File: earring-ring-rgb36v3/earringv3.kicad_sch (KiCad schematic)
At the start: 60 parts, among them J1 Conn_01x05, SW1 SW_Push, SW2 SW_Push, U1 STM32U073KCUx, U2 GMA2718H09-F42-4P

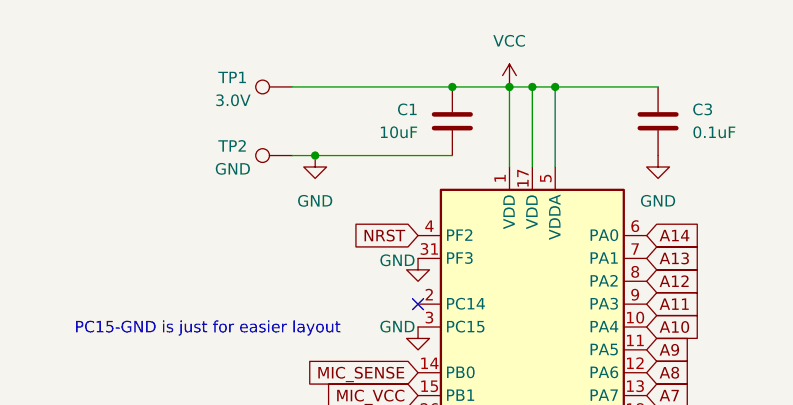
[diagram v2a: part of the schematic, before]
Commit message: earring-ring-rgb36v3: add extra capacitor
The datasheet says this capacitor is needed so :shrug:
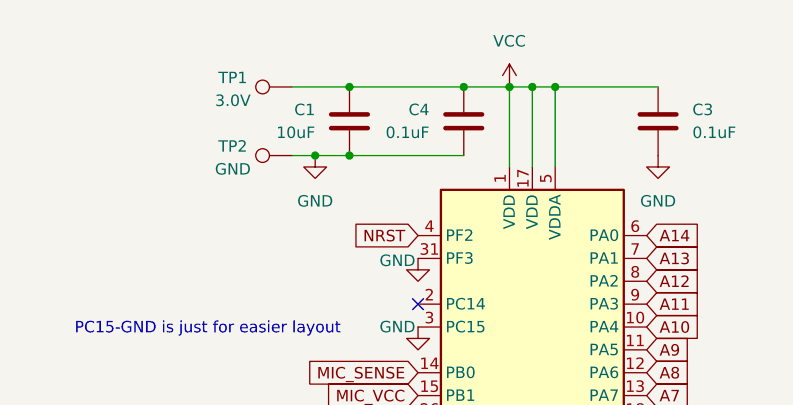
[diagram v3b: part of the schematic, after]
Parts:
- added C4: 0.1uF, Capacitor_SMD:C_0402_1005Metric, symbol Device:C
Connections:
- net GND: now also C4.2
- net VCC: now also C4.1
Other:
- moved on the sheet: C1
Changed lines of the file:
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@@
 	)
 	(junction
-		(at 57.15 22.86)
+		(at 58.42 22.86)
 		(diameter 0)
 		(color 0 0 0 0)
@@
 	)
 	(junction
+		(at 45.72 30.48)
+		(diameter 0)
+		(color 0 0 0 0)
+	)
+	(junction
+		(at 45.72 22.86)
+		(diameter 0)
+		(color 0 0 0 0)
+	)
+	(junction
 		(at 63.5 22.86)
 		(diameter 0)
@@
 	(wire
 		(pts
-			(xy 39.37 22.86) (xy 57.15 22.86)
+			(xy 39.37 22.86) (xy 45.72 22.86)
+		)
+		(stroke
+			(width 0)
+			(type default)
+		)
+	)
+	(wire
+		(pts
+			(xy 45.72 22.86) (xy 58.42 22.86)
 		)
 		(stroke
@@
 	(wire
 		(pts
+			(xy 58.42 22.86) (xy 63.5 22.86)
+		)
+		(stroke
+			(width 0)
+			(type default)
+		)
+	)
+	(wire
+		(pts
 			(xy 68.58 22.86) (xy 80.01 22.86)
 		)
@@
 	(wire
 		(pts
-			(xy 39.37 62.23) (xy 39.37 99.06)
+			(xy 45.72 30.48) (xy 58.42 30.48)
 		)
 		(stroke
@@
 	(wire
 		(pts
-			(xy 68.58 156.21) (xy 69.85 156.21)
+			(xy 39.37 62.23) (xy 39.37 99.06)
 		)
 		(stroke
@@
 	(wire
 		(pts
-			(xy 39.37 99.06) (xy 45.72 99.06)
+			(xy 68.58 156.21) (xy 69.85 156.21)
 		)
 		(stroke
@@
 	(wire
 		(pts
-			(xy 66.04 22.86) (xy 68.58 22.86)
+			(xy 39.37 99.06) (xy 45.72 99.06)
 		)
 		(stroke
@@
 	(wire
 		(pts
-			(xy 45.72 59.69) (xy 45.72 87.63)
+			(xy 66.04 22.86) (xy 68.58 22.86)
 		)
 		(stroke
@@
 	(wire
 		(pts
-			(xy 55.88 99.06) (xy 66.04 99.06)
+			(xy 45.72 59.69) (xy 45.72 87.63)
 		)
 		(stroke
@@
 	(wire
 		(pts
-			(xy 55.88 87.63) (xy 66.04 87.63)
+			(xy 55.88 99.06) (xy 66.04 99.06)
 		)
 		(stroke
@@
 	(wire
 		(pts
-			(xy 39.37 30.48) (xy 41.91 30.48)
+			(xy 55.88 87.63) (xy 66.04 87.63)
 		)
 		(stroke
@@
 	(wire
 		(pts
-			(xy 57.15 22.86) (xy 63.5 22.86)
+			(xy 39.37 30.48) (xy 41.91 30.48)
 		)
 		(stroke
@@
 	(wire
 		(pts
-			(xy 41.91 30.48) (xy 57.15 30.48)
+			(xy 41.91 30.48) (xy 45.72 30.48)
 		)
 		(stroke
@@
 	)
 	(symbol
+		(lib_id "Device:C")
+		(at 58.42 26.67 0)
+		(mirror y)
+		(unit 1)
+		(exclude_from_sim no)
+		(in_bom yes)
+		(on_board yes)
+		(dnp no)
+		(property "Reference" "C4"
+			(at 54.61 25.3999 0)
+			(effects
+				(font
+					(size 1.27 1.27)
+				)
+				(justify left)
+			)
+		)
+		(property "Value" "0.1uF"
+			(at 54.61 27.9399 0)
+			(effects
+				(font
+					(size 1.27 1.27)
+				)
+				(justify left)
+			)
+		)
+		(property "Footprint" "Capacitor_SMD:C_0402_1005Metric"
+			(at 57.4548 30.48 0)
+			(effects
+				(font
+					(size 1.27 1.27)
+				)
+				(hide yes)
+			)
+		)
+		(property "Datasheet" "~"
+			(at 58.42 26.67 0)
+			(effects
+				(font
+					(size 1.27 1.27)
+				)
+				(hide yes)
+			)
+		)
+		(property "Description" "Unpolarized capacitor"
+			(at 58.42 26.67 0)
+			(effects
+				(font
+					(size 1.27 1.27)
+				)
+				(hide yes)
+			)
+		)
+		(property "LCSC" "C1525"
+			(at 58.42 26.67 0)
+			(effects
+				(font
+					(size 1.27 1.27)
+				)
+				(hide yes)
+			)
+		)
+		(pin "1"
+		)
+		(pin "2"
+		)
+		(instances
+			(project "earringv3"
+				(path "/5b672b97-2486-4be1-9927-7141d9b63fb2"
+					(reference "C4")
+					(unit 1)
+				)
+			)
+		)
+	)
+	(symbol
 		(lib_id "MCU_ST_STM32U0:STM32U073KCUx")
 		(at 66.04 59.69 0)
@@
 	(symbol
 		(lib_id "Device:C")
-		(at 57.15 26.67 0)
+		(at 45.72 26.67 0)
 		(mirror y)
 		(unit 1)
@@
 		(dnp no)
 		(property "Reference" "C1"
-			(at 53.34 25.3999 0)
+			(at 41.91 25.3999 0)
 			(effects
 				(font
@@
 		)
 		(property "Value" "10uF"
-			(at 53.34 27.9399 0)
+			(at 41.91 27.9399 0)
 			(effects
 				(font
@@
 		)
 		(property "Footprint" "Capacitor_SMD:C_0402_1005Metric"
-			(at 56.1848 30.48 0)
+			(at 44.7548 30.48 0)
 			(effects
 				(font
@@
 		)
 		(property "Datasheet" "~"
-			(at 57.15 26.67 0)
+			(at 45.72 26.67 0)
 			(effects
 				(font
@@
 		)
 		(property "Description" "Unpolarized capacitor"
-			(at 57.15 26.67 0)
+			(at 45.72 26.67 0)
 			(effects
 				(font
@@
 		)
 		(property "LCSC" "C15525"
-			(at 57.15 26.67 0)
+			(at 45.72 26.67 0)
 			(effects
 				(font

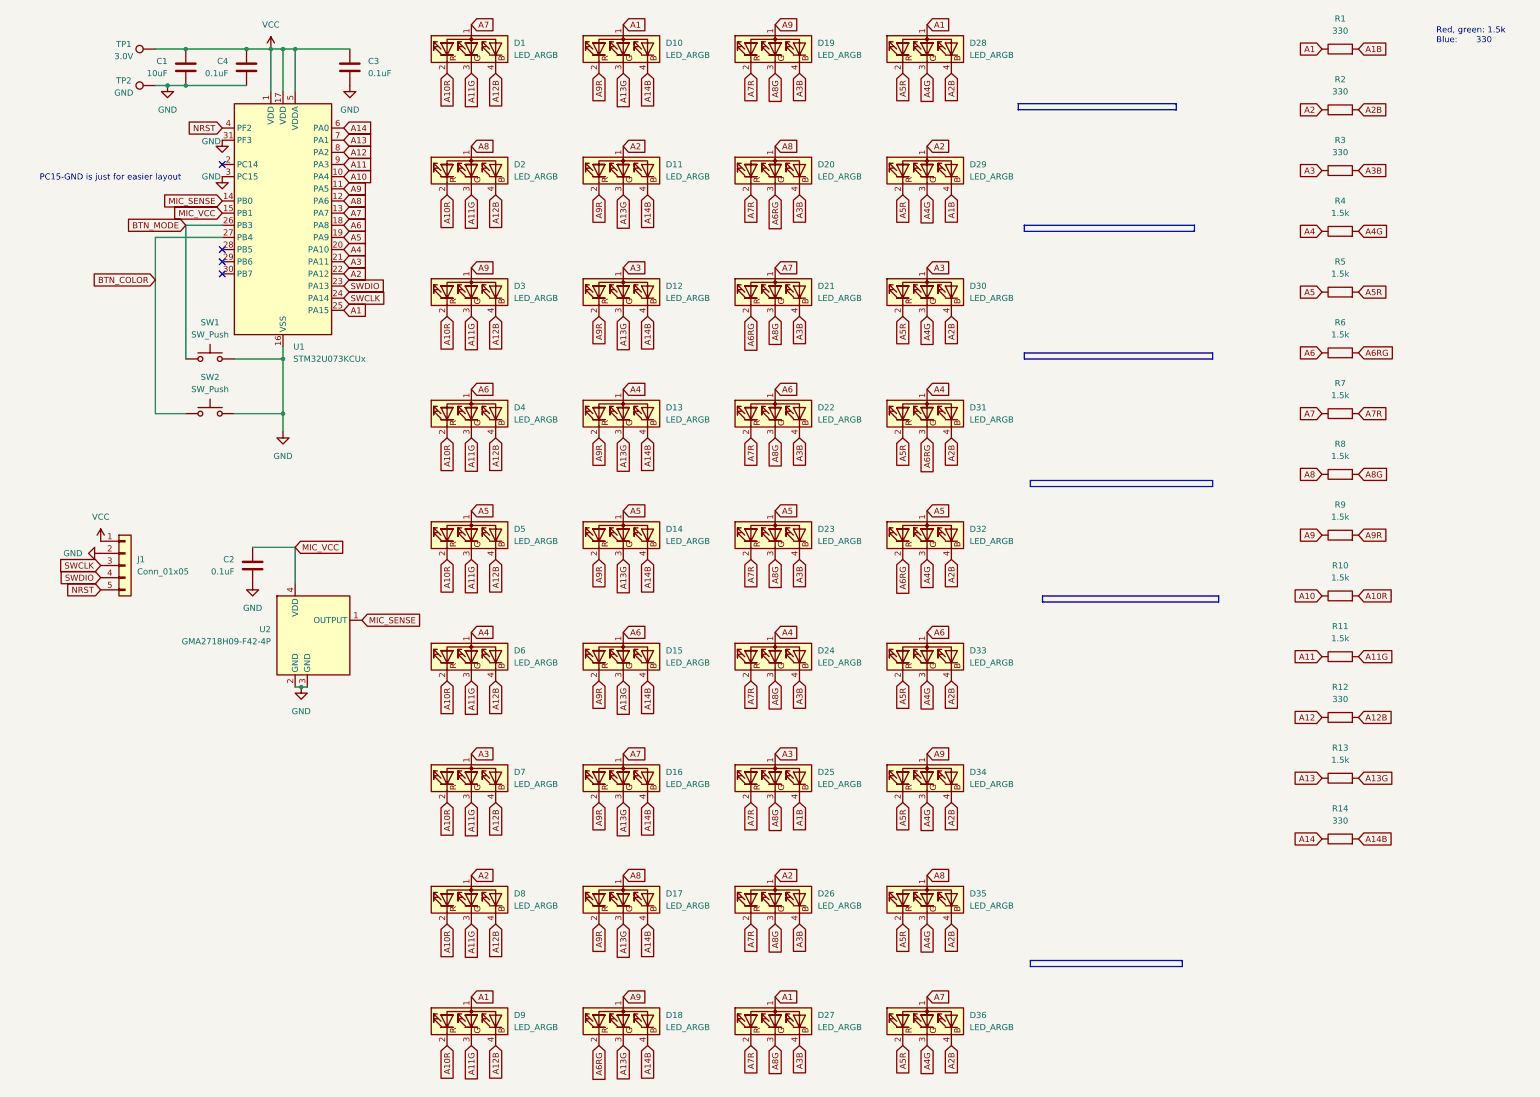
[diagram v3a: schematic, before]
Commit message: earring-ring-rgb36v3: prepare for ordering
  * Replace main MCU with a cheaper (in bulk) variant.
    (that is also in stock at JLCPCB)
  * Fix main MCU orientation (it's rotated differently at JLCPCB)
  * Replace red and green LED resistor with a higher value.
    Blue tends to be slightly dimmer, this might help with that.
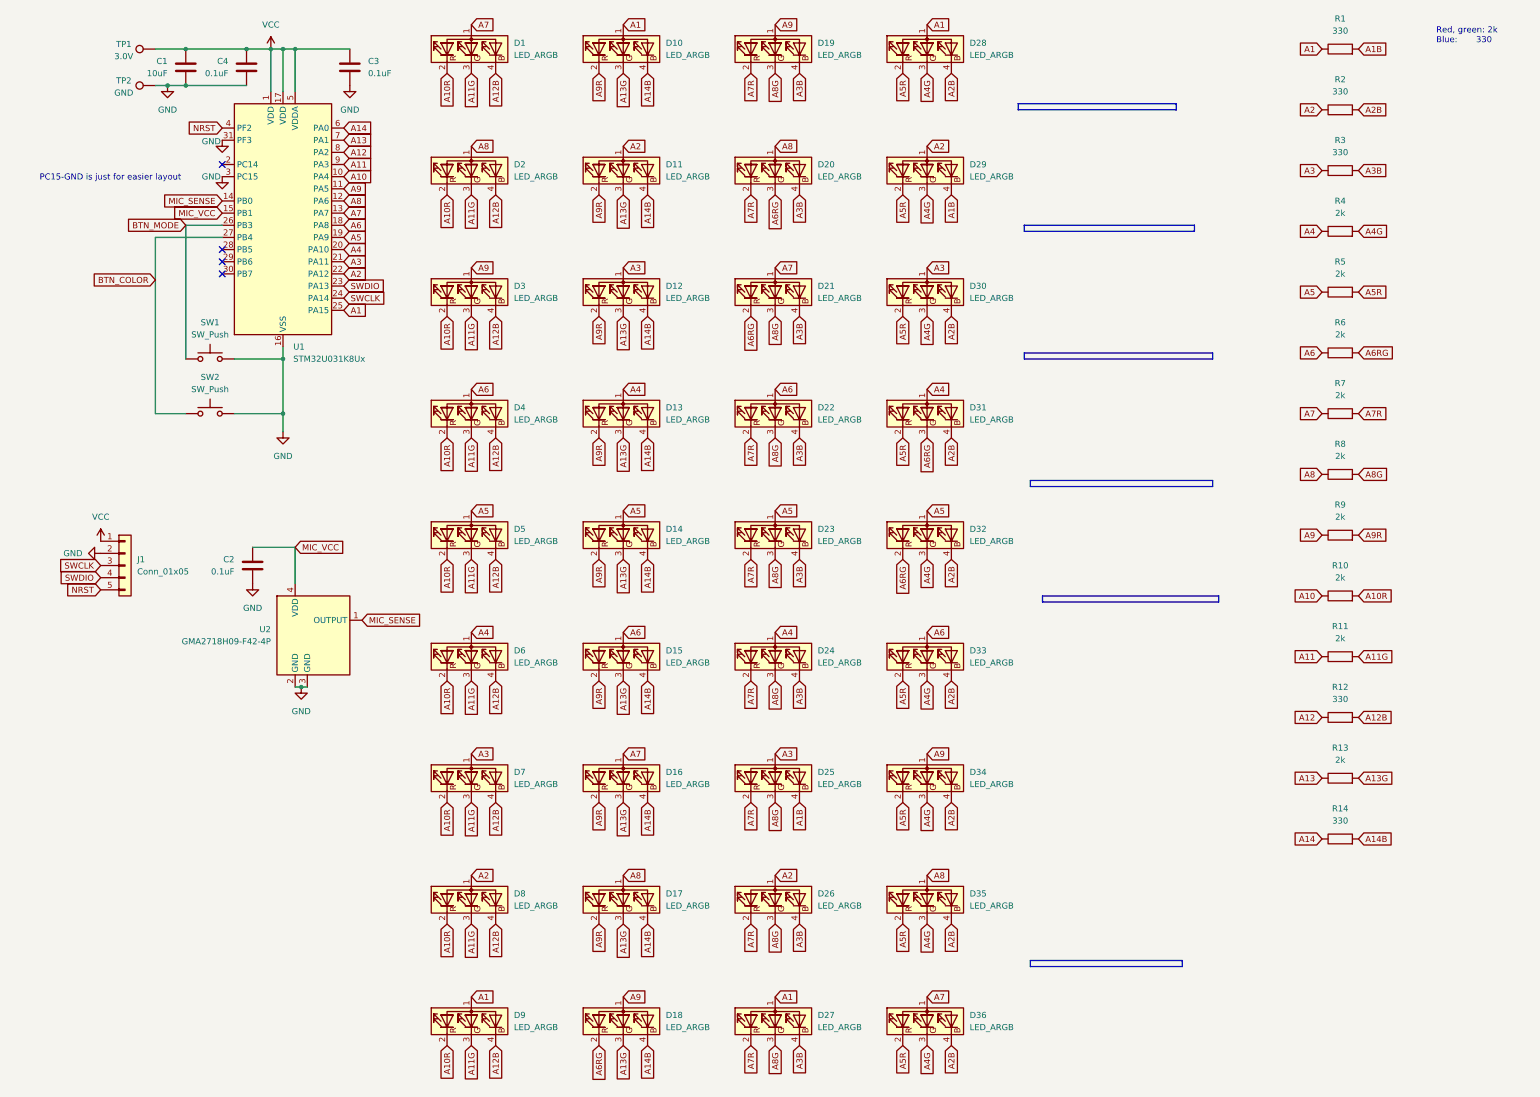
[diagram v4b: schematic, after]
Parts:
- removed U1: STM32U073KCUx, Package_DFN_QFN:QFN-32-1EP_5x5mm_P0.5mm_EP3.45x3.45mm, symbol MCU_ST_STM32U0:STM32U073KCUx
- added U1: STM32U031K8Ux, Package_DFN_QFN:QFN-32-1EP_5x5mm_P0.5mm_EP3.45x3.45mm, symbol MCU_ST_STM32U0:STM32U031K8Ux
- R10, R11, R13, R4, R5, R6, R7, R8, R9: value 1.5k -> 2k; LCSC C25867 -> C4109
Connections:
- net A1: now also U1.25 (PA15)
- net A10: now also U1.10 (PA4)
- net A11: now also U1.9 (PA3)
- net A12: now also U1.8 (PA2)
- net A13: now also U1.7 (PA1)
- net A14: now also U1.6 (PA0)
- net A2: now also U1.22 (PA12)
- net A3: now also U1.21 (PA11)
- net A4: now also U1.20 (PA10)
- net A5: now also U1.19 (PA9)
- net A6: now also U1.18 (PA8)
- net A7: now also U1.13 (PA7)
- net A8: now also U1.12 (PA6)
- net A9: now also U1.11 (PA5)
- net BTN_COLOR: now also U1.27 (PB4)
- net BTN_MODE: now also U1.26 (PB3)
- net GND: now also U1.16 (VSS), U1.3 (PC15), U1.31 (PF3), U1.32 (VSS), U1.33 (VSS)
- net MIC_SENSE: now also U1.14 (PB0)
- net MIC_VCC: now also U1.15 (PB1)
- net NRST: now also U1.4 (PF2)
- net SWCLK: now also U1.24 (PA14)
- net SWDIO: now also U1.23 (PA13)
- net VCC: now also U1.1 (VDD), U1.17 (VDD), U1.5 (VDDA)
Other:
- note added: "Red, green: 2k Blue: 330"
- note removed: "Red, green: 1.5k Blue: 330"
